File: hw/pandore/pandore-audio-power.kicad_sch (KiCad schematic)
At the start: 82 parts, among them J22 V12ISO, J23 AV5, J24 AV3P3, Q7 MOSFET_EN-N, U12 NXES2, U13 LDL212DR, U14 LDL212DR, U21 LM5158, U22 TPS7A4001

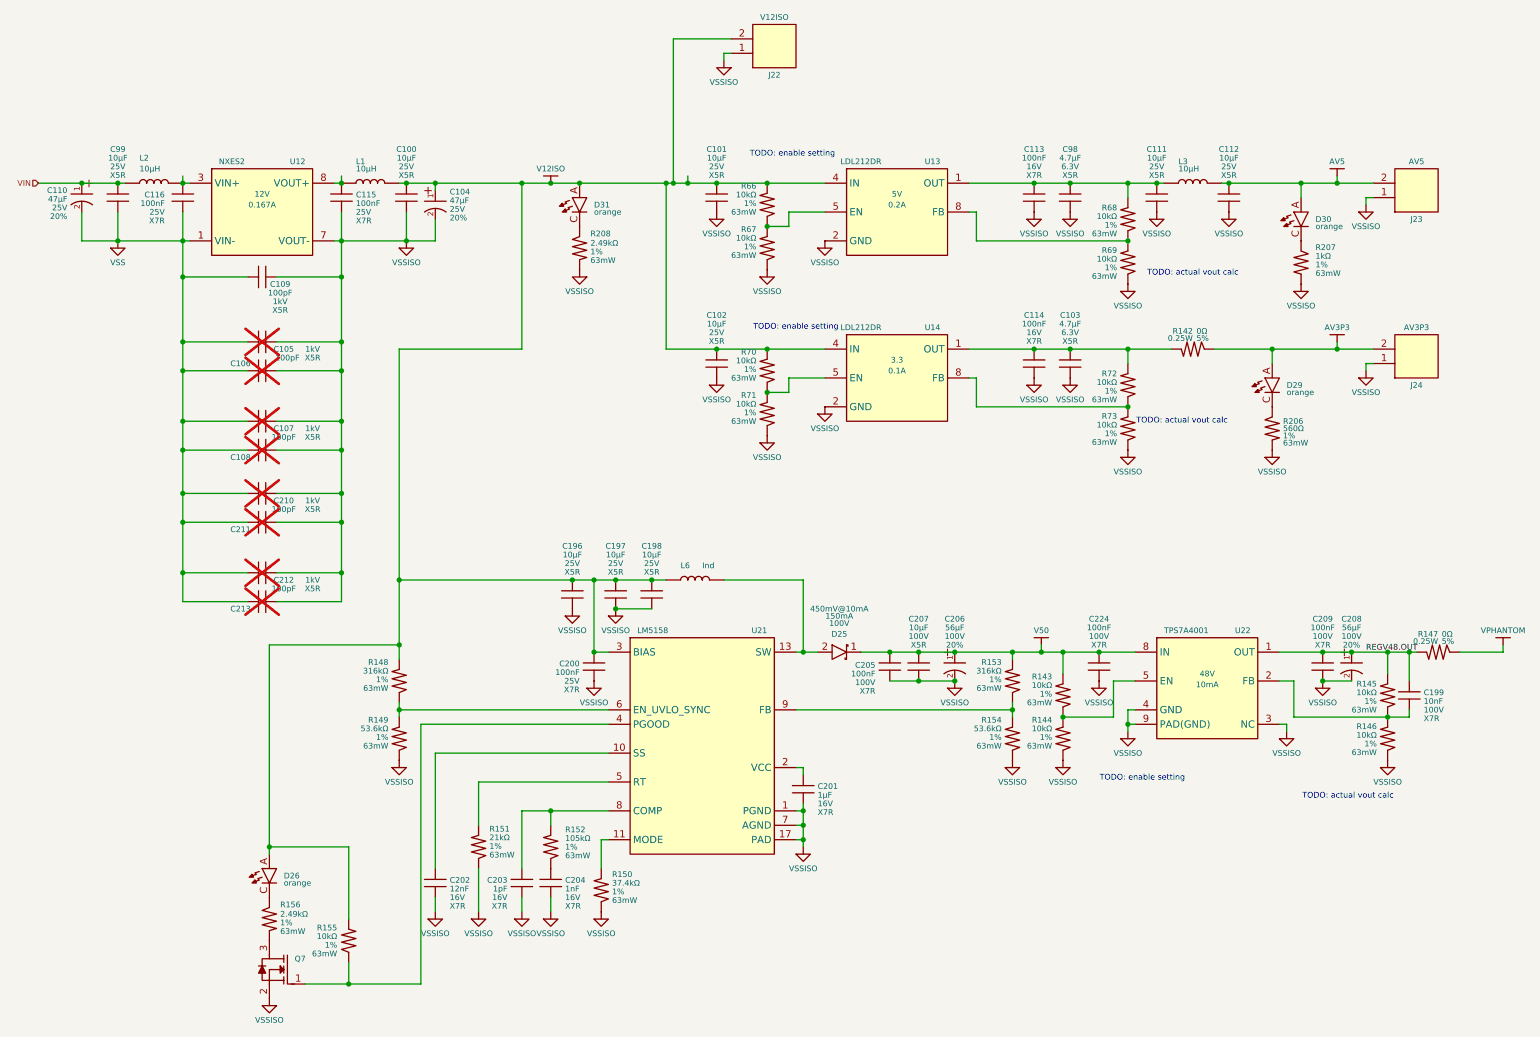
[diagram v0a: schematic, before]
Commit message: finished adding mpn,mfg to all parts, finished routing placement
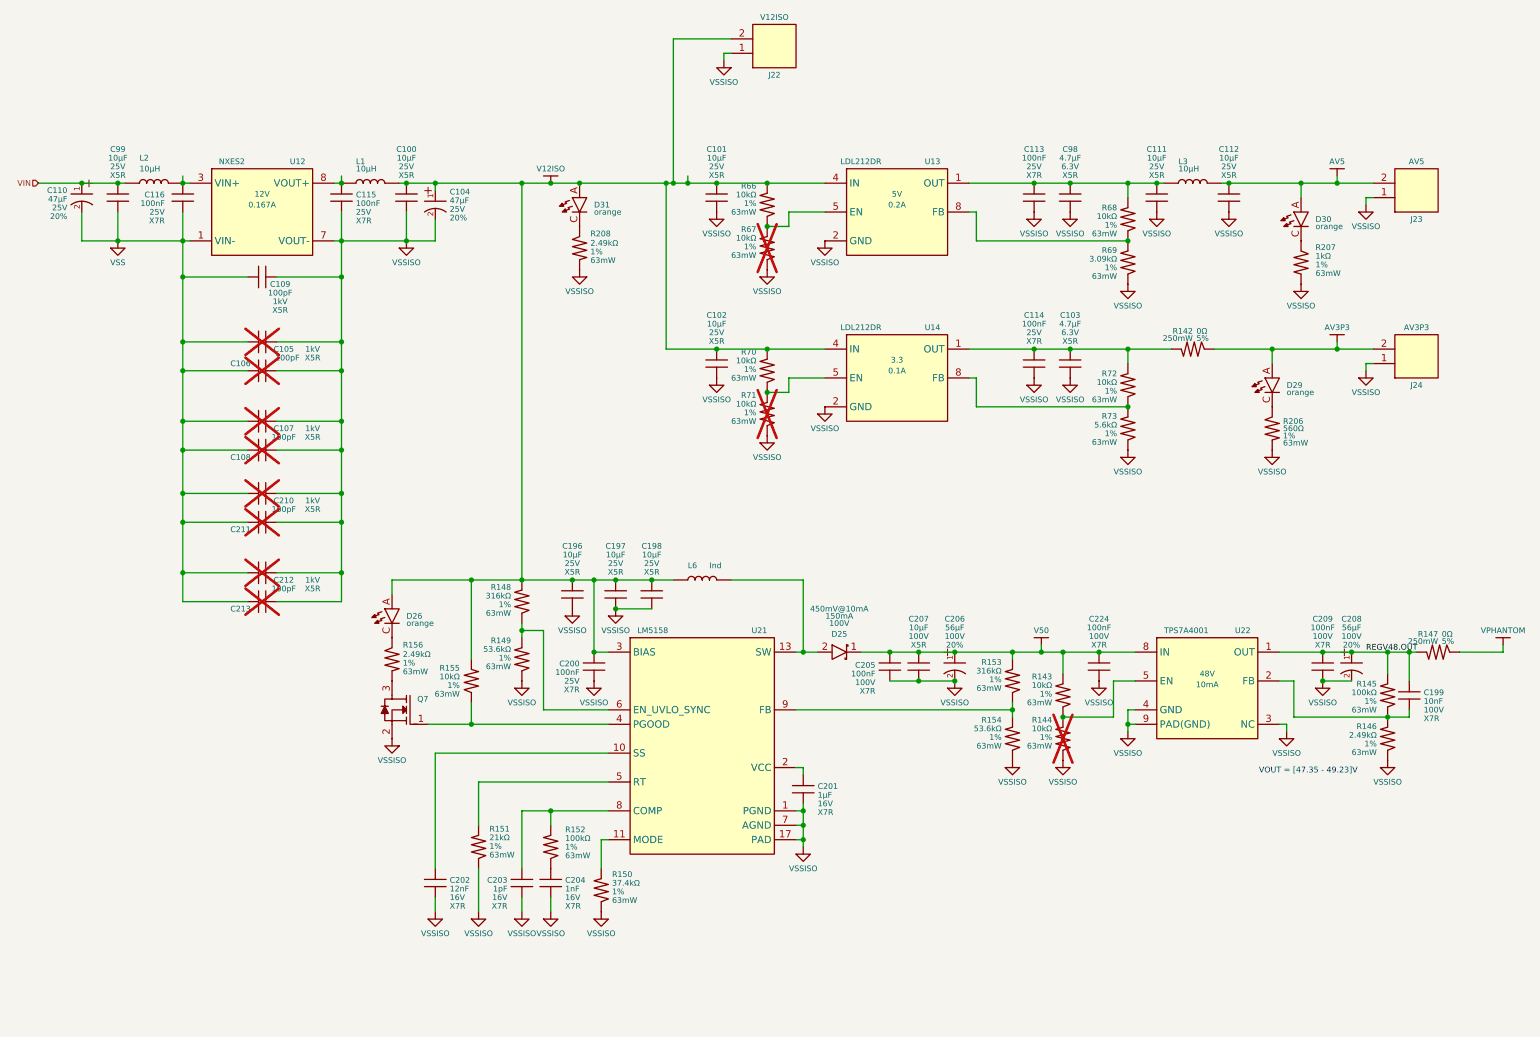
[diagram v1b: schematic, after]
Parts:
- C100, C101, C102, C111, C112, C196, C197, C198, C99: MFG (none) -> Murata; MPN (none) -> GRM21BR61E106KA73K
- C105, C106, C107, C108, C109, C210, C211, C212, C213: MFG (none) -> Vishay Vitramon; MPN (none) -> VJ1206A101JXGCW1HV
- C113, C114: MFG2 Samsung Electro-Mechanics -> (none); MFG3 Taiyo Yuden -> (none); MPN2 CL05B104KA5NNNC -> (none); MPN3 EMK105B7104KV-F -> (none); Voltage 16V -> 25V
- C115, C116, C200: Link (none) -> https://www.passivecomponent.com/product-search/MLCC/?partn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; MFG (none) -> Walsin Technology Corporation; MPN (none) -> 0402B104K160CT
- C199: MFG (none) -> Murata; MPN (none) -> GCM188R72A103KA37D
- C201: MFG (none) -> KEMET; MPN (none) -> C0603C105K4RACTU
- C202: MFG (none) -> Murata; MPN (none) -> GCM155R71E123KA55J
- C203: Link (none) -> https://yageogroup.com/products/Capacitors/part/CC0402BRNPO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; MFG (none) -> Yageo; MPN (none) -> CC0402BRNPO9BN1R0
- C204: Link (none) -> https://yageogroup.com/products/Capacitors/part/CC0402KRX7R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; MFG (none) -> Yageo; MPN (none) -> CC0402KRX7R9BB102
- C205, C209, C224: MFG (none) -> Samsung Electro-Mechanics; MPN (none) -> CL21B104KCFNNNE
- C207: MFG (none) -> Murata; MPN (none) -> GRM32EC72A106ME05K
- J22, J23: MFG (none) -> Adam Tech; MPN (none) -> PH1-02-UA
- J24: Link https://www.we-online.com/en/components/products/TBL_5_00_1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 -> (none); MFG (none) -> Adam Tech; MPN (none) -> PH1-02-UA
- R142, R147: Link (none) -> https://yageogroup.com/products/Resistors/part/RT0805DRE074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; MFG (none) -> YAGEO; MPN (none) -> RC0805JR-070RL; Power 0.25W -> 250mW
- R144, R67, R71: now not fitted
- R145: Link https://www.bourns.com/search?indexCatalogue=psindex&search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 -> https://yageogroup.com/products/Resistors/part/RC0402FR-079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; MFG Bourns Inc -> YAGEO; MFG2 Walsin Technology Corporation -> (none); MFG3 Yageo -> (none); MPN CR0402-FX-1002GLF -> RC0402FR-07100KL; MPN2 WR04X1002FTL -> (none); MPN3 RC0402FR-0710KL -> (none); Resistance 10kΩ -> 100kΩ
- R146: Link https://www.bourns.com/search?indexCatalogue=psindex&search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 -> https://yageogroup.com/products/Resistors/part/RC0402FR-132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; MFG Bourns Inc -> YAGEO; MFG2 Walsin Technology Corporation -> (none); MFG3 Yageo -> (none); MPN CR0402-FX-1002GLF -> RC0402FR-132K49L; MPN2 WR04X1002FTL -> (none); MPN3 RC0402FR-0710KL -> (none); Resistance 10kΩ -> 2.49kΩ
- R148, R153: Link (none) -> https://yageogroup.com/products/Resistors/part/RC0402FR-073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; MFG Bourns I -> YAGEO; MPN (none) -> RC0402FR-07316KL
- R149, R154: Link (none) -> https://yageogroup.com/products/Resistors/part/RC0402FR-075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; MFG (none) -> YAGEO; MPN CR0402-FX-1002GL -> RC0402FR-0753K6L
- R150: Link (none) -> https://yageogroup.com/products/Resistors/part/RC0402FR-073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; MFG (none) -> YAGEO; MPN (none) -> RC0402FR-0737K4L
- R151: Link (none) -> https://yageogroup.com/products/Resistors/part/RC0402FR-072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; MFG (none) -> YAGEO; MPN (none) -> RC0402FR-0721KL
- R152: Link (none) -> https://yageogroup.com/products/Resistors/part/RC0402FR-079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; MFG (none) -> YAGEO; MPN (none) -> RC0402FR-07100KL; Resistance 105kΩ -> 100kΩ
- R156, R208: Link (none) -> https://yageogroup.com/products/Resistors/part/RC0402FR-132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; MFG (none) -> YAGEO; MPN (none) -> RC0402FR-132K49L
- R206: Link (none) -> https://yageogroup.com/products/Resistors/part/RC0402FR-075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; MFG (none) -> YAGEO; MPN (none) -> RC0402FR-07560RL
- R207: Link (none) -> https://yageogroup.com/products/Resistors/part/RC0402FR-131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; MFG (none) -> YAGEO; MPN (none) -> RC0402FR-131KL
- R69: Link https://www.bourns.com/search?indexCatalogue=psindex&search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 -> https://yageogroup.com/products/Resistors/part/RC0402FR-073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; MFG Bourns Inc -> YAGEO; MFG2 Walsin Technology Corporation -> (none); MFG3 Yageo -> (none); MPN CR0402-FX-1002GLF -> RC0402FR-073K09L; MPN2 WR04X1002FTL -> (none); MPN3 RC0402FR-0710KL -> (none); Resistance 10kΩ -> 3.09kΩ
- R73: Link https://www.bourns.com/search?indexCatalogue=psindex&search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 -> https://yageogroup.com/products/Resistors/part/RC0402FR-075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; MFG Bourns Inc -> YAGEO; MFG2 Walsin Technology Corporation -> (none); MFG3 Yageo -> (none); MPN CR0402-FX-1002GLF -> RC0402FR-075K6L; MPN2 WR04X1002FTL -> (none); MPN3 RC0402FR-0710KL -> (none); Resistance 10kΩ -> 5.6kΩ
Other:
- note added: "VOUT = [47.35 - 49.23]V"
- note removed: "TODO: actual vout calc"
- note removed: "TODO: enable setting"
- moved on the sheet: D26, L6, Q7, R148, R149, R155, R156
